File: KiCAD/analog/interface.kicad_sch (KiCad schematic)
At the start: 11 parts, among them J15 Conn_01x03_Pin, J4 8P8C_Shielded, U16 AM26LS32ACN

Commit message: schematic: revB encoder interrupt rerouted through CAT6 umbilical
- interface.kicad_sch: ENC_INT global label (input) replaces the old
  direct wire+GND stub; encoder interrupt now travels over the RJ45
  cable with the shield as signal return
- frontpanel.kicad_sch: 4-pin header J (Conn_01x04) added for up to
  3 encoder connections + one test-point pin; ENC_INT_IN label wired in
- arduino.kicad_sch: removed orphaned Conn_Coaxial symbol cache
- vfo.kicad_sch: minor layout/annotation updates

Co-Authored-By: Claude Sonnet 4.6 (1M context) <noreply@anthropic.com>
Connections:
- net GND: no longer J4.5
- new net ENC_INT: J4.5
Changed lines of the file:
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@@
 	(wire
 		(pts
-			(xy 64.77 91.44) (xy 64.77 95.25)
+			(xy 139.7 113.03) (xy 149.86 113.03)
 		)
 		(stroke
@@
 	(wire
 		(pts
-			(xy 139.7 113.03) (xy 149.86 113.03)
+			(xy 170.18 92.71) (xy 142.24 92.71)
 		)
 		(stroke
@@
 	(wire
 		(pts
-			(xy 170.18 92.71) (xy 142.24 92.71)
+			(xy 35.56 96.52) (xy 58.42 96.52)
 		)
 		(stroke
@@
 	(wire
 		(pts
-			(xy 35.56 96.52) (xy 58.42 96.52)
+			(xy 142.24 92.71) (xy 137.16 92.71)
 		)
 		(stroke
@@
 	(wire
 		(pts
-			(xy 142.24 92.71) (xy 137.16 92.71)
+			(xy 153.67 97.79) (xy 151.13 97.79)
 		)
 		(stroke
@@
 	(wire
 		(pts
-			(xy 153.67 97.79) (xy 151.13 97.79)
+			(xy 151.13 105.41) (xy 151.13 97.79)
 		)
 		(stroke
@@
 	(wire
 		(pts
-			(xy 151.13 105.41) (xy 151.13 97.79)
+			(xy 35.56 88.9) (xy 82.55 88.9)
 		)
 		(stroke
@@
 	(wire
 		(pts
-			(xy 35.56 88.9) (xy 82.55 88.9)
+			(xy 60.96 71.12) (xy 83.82 71.12)
 		)
 		(stroke
@@
 	(wire
 		(pts
-			(xy 60.96 71.12) (xy 83.82 71.12)
+			(xy 58.42 135.89) (xy 91.44 135.89)
 		)
 		(stroke
@@
 	(wire
 		(pts
-			(xy 58.42 135.89) (xy 91.44 135.89)
+			(xy 142.24 97.79) (xy 137.16 97.79)
 		)
 		(stroke
@@
 	(wire
 		(pts
-			(xy 142.24 97.79) (xy 137.16 97.79)
+			(xy 58.42 96.52) (xy 58.42 135.89)
 		)
 		(stroke
@@
 	(wire
 		(pts
-			(xy 58.42 96.52) (xy 58.42 135.89)
+			(xy 170.18 105.41) (xy 151.13 105.41)
 		)
 		(stroke
@@
 	(wire
 		(pts
-			(xy 170.18 105.41) (xy 151.13 105.41)
+			(xy 77.47 83.82) (xy 77.47 78.74)
 		)
 		(stroke
@@
 		)
 	)
-	(wire
-		(pts
-			(xy 35.56 91.44) (xy 64.77 91.44)
-		)
-		(stroke
-			(width 0)
-			(type default)
-		)
-	)
-	(wire
-		(pts
-			(xy 77.47 83.82) (xy 77.47 78.74)
-		)
-		(stroke
-			(width 0)
-			(type default)
-		)
-	)
 	(global_label "MBL_B_P"
 		(shape output)
@@
 					(size 1.27 1.27)
 				)
+			)
+		)
+	)
+	(global_label "ENC_INT"
+		(shape input)
+		(at 35.56 91.44 0)
+		(fields_autoplaced yes)
+		(effects
+			(font
+				(size 1.27 1.27)
+			)
+			(justify left)
+		)
+		(property "Intersheetrefs" "${INTERSHEET_REFS}"
+			(at 46.1652 91.44 0)
+			(hide yes)
+			(show_name no)
+			(do_not_autoplace no)
+			(effects
+				(font
+					(size 1.27 1.27)
+				)
+				(justify left)
 			)
 		)
@@
 					(unit 1)
 				)
-			)
-		)
-	)
-	(symbol
-		(lib_id "power:GND")
-		(at 64.77 95.25 0)
-		(unit 1)
-		(body_style 1)
-		(exclude_from_sim no)
-		(in_bom yes)
-		(on_board yes)
-		(in_pos_files yes)
-		(dnp no)
-		(fields_autoplaced yes)
-		(property "Reference" "#PWR090"
-			(at 64.77 101.6 0)
-			(hide yes)
-			(show_name no)
-			(do_not_autoplace no)
-			(effects
-				(font
-					(size 1.27 1.27)
-				)
-			)
-		)
-		(property "Value" "GND"
-			(at 64.77 100.33 0)
-			(show_name no)
-			(do_not_autoplace no)
-			(effects
-				(font
-					(size 1.27 1.27)
-				)
-			)
-		)
-		(property "Footprint" ""
-			(at 64.77 95.25 0)
-			(hide yes)
-			(show_name no)
-			(do_not_autoplace no)
-			(effects
-				(font
-					(size 1.27 1.27)
-				)
-			)
-		)
-		(property "Datasheet" ""
-			(at 64.77 95.25 0)
-			(hide yes)
-			(show_name no)
-			(do_not_autoplace no)
-			(effects
-				(font
-					(size 1.27 1.27)
-				)
-			)
-		)
-		(property "Description" "Power symbol creates a global label with name \"GND\" , ground"
-			(at 64.77 95.25 0)
-			(hide yes)
-			(show_name no)
-			(do_not_autoplace no)
-			(effects
-				(font
-					(size 1.27 1.27)
-				)
-			)
-		)
-		(pin "1"
-		)
-		(instances
-			(project "analog"
-				(path "/d3de40b8-856b-4fbd-829c-f45ffcd55742/5c3f4a2b-7d1e-4f8b-9c6d-0e8a1b2c3d4e"
-					(reference "#PWR090")
-					(unit 1)
-				)

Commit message: kicad: fix AM26LS32ACN (U16) symbol pin assignments
Correct four pin numbers that were wrong in both the library symbol
and the interface.kicad_sch embedded lib_symbols copy:

  1B: 3 -> 1   1Y: 1 -> 3
  4B: 13 -> 15  4Y: 15 -> 13

1A (pin 2), 4A (pin 14), and all other pins were correct.
RevB PCB layout will pick up the corrected netlist automatically.

Co-Authored-By: Claude Sonnet 4.6 <noreply@anthropic.com>
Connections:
- net MBL_A_N: now also U16.1 (1B); no longer U16.3 (1B)
- net at R26.1: now also U16.3 (1Y); no longer U16.1 (1Y)

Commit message: KiCad revB: protoshield schematic complete + 1N4728A symbol + misc board edits
Protoshield (Metro ESP32-S3 GPIO signal conditioning):
- Full schematic drawn: series R + bypass C + Zener clamp for I_CATHODE_A/B
  (1k+100nF+1N4728A), MBL600_A/B (10k/20k divider + 22pF), GRID_BLOCK_CRASH
  (1k+100nF), ENC_INT (330R+10k pull-up), PADDLE_A/B (10k pull-ups), RESET_N
  (100nF), TR_SENSE (10k pull-up), passthrough nodes for SPI and LDAC_4728
- All THT footprints assigned (ceramic disc caps, DIN0207 resistors, Phoenix
  MKDS-1.5 2-pin/3-pin terminal blocks)
- ENC_INT wiring gap fixed (R7 re-placed to connect J4 pin 2 to ENC_INT net)
- sym-lib-table added (points to shared xmitter.kicad_sym)
- protoshield.net generated netlist added for reference

Symbol library (xmitter.kicad_sym):
- Added 1N4728A (3.3V 1W Zener, DO-41) with correct KiCad 9.0 inline pts format

Other boards:
- analog/arduino.kicad_sch: minor junction/reference adjustments after Metro
  symbol was removed to protoshield in prior session
- bias: kicad_pro and kicad_sch updated (ongoing schematic work)
- power/sym-lib-table added for new stub project

Added: Purchase Orders (JLCPCB + Digi-Key invoices), tools/_scan_symbols.py

Co-Authored-By: Claude Sonnet 4.6 <noreply@anthropic.com>
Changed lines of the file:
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@@
 		(in_pos_files yes)
 		(dnp no)
-		(fields_autoplaced yes)
 		(property "Reference" "#PWR099"
 			(at 142.24 111.76 0)
@@
 		)
 		(property "Value" "GND"
-			(at 142.24 110.49 0)
+			(at 145.796 108.204 0)
 			(show_name no)
 			(do_not_autoplace no)

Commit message: KiCad revB: schematic review pass — I2C, ENC_INT, GND returns, GRID_BLOCK_CRASH clamp
Result of extended review pass against fresh netlists across all four
boards. All connectivity blockers resolved.

- Si5351 SDA/SCL wired via 0R jumpers (R8/R9) puts I2C on PCB traces
  for PCF8575 U17 and the RJ45 to the front panel. MCP4728 side has
  parallel 0R jumpers (R3/R4/R5) left DNP by default — STEMMA-QT is
  the intended path.
- ENC_INT chain unified end-to-end with staged names:
  ENC_INT_RAW (frontpanel encoder wire-OR) → ENC_INT_CLEAN (across
  CAT + analog pass-through) → ENC_INT_FINAL (post-protoshield
  conditioning). Frontpanel U4 (MCP1700-3.3 LDO) sources the +3.3V
  the pull-up R4 needs; pull-up moved to encoder side for sharper
  falling edges over the 2 m CAT run.
- Protoshield GRID_BLOCK_CRASH gets 1N4728A Zener clamp (D5),
  matching the I_CATHODE and MBL600 5V→3.3V clamp topology.
- Protoshield MBL600 conditioning rebuilt: 1K series + 100nF filter
  + 1N4728A clamp (was 10K/20K divider + 22pF that filtered nothing
  below RF).
- PADDLE_A/B and RESET_N removed from analog board — case-mounted
  switches wire directly to protoshield.
- Protoshield J1/J6 widened to 3-pin to include GND returns for the
  case-mounted paddle and reset switches.
- Bias board reference designators reorganized functionally
  (R_FA/R_FB feedback, R_GA/R_GB gain, R_PADA/R_PADB, R_GLA/R_GLB
  grid line, R_GATE, R_Z).
- New Documentation/control_board_functional_blocks.md captures
  KeyUp/Gate 2 keying, relay assignments (J6=T/R, J7=HV primary,
  J8=HV inrush), CD14538B heartbeat watchdog, TR_SENSE interlock,
  and J13 power-migration header.
- Fresh netlists exported for all four boards.

Co-Authored-By: Claude Opus 4.7 <noreply@anthropic.com>
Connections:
- net ENC_INT renamed ENC_INT_CLEAN
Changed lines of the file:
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@@
 		)
 	)
-	(global_label "ENC_INT"
-		(shape input)
+	(global_label "ENC_INT_CLEAN"
+		(shape output)
 		(at 35.56 91.44 0)
 		(fields_autoplaced yes)
@@
 		)
 		(property "Intersheetrefs" "${INTERSHEET_REFS}"
-			(at 46.1652 91.44 0)
+			(at 52.999 91.44 0)
 			(hide yes)
 			(show_name no)

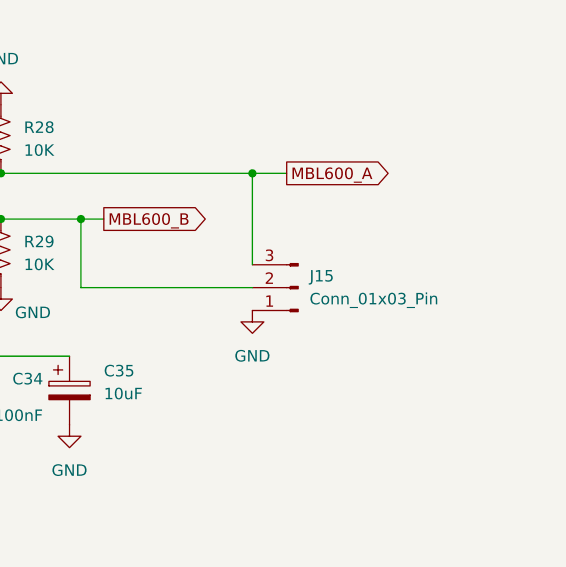
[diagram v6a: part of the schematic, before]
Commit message: revC: accumulated schematic/netlist updates + BOM tooling
- analog + ss_pa netlists regenerated to current schematic state
- interface/arduino/dac/power sheet updates on analog
- fault_shutdown and pa_stage edits on ss_pa (footprint assignments)
- assign_cap_footprints.py: additional VALUE_TO_FOOTPRINT entries
- gen_board_boms.py: per-board BOM generator (multi-sheet .xlsx by
  component category, first-match-wins bucketing, DNP exclusion)
- gen_total_bom.py: consolidated BOM across analog + frontpanel + ss_pa
  for a single Mouser order, board-prefixed references, mixed-footprint
  flagging per Value row

Co-Authored-By: Claude Opus 4.7 <noreply@anthropic.com>
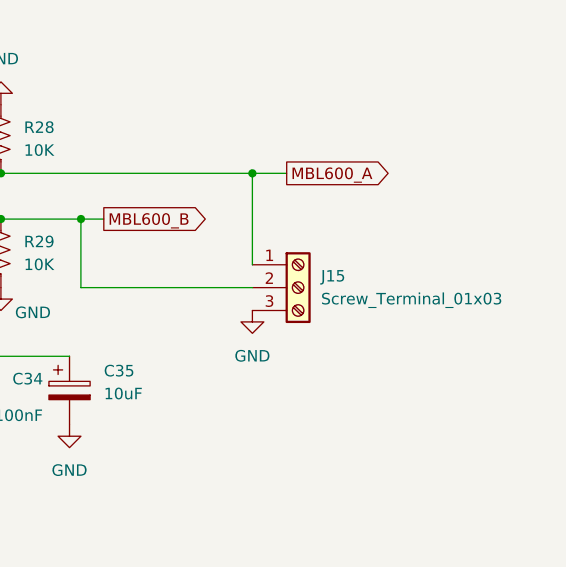
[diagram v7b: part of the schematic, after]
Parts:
- removed J15: Conn_01x03_Pin, Connector_PinHeader_2.54mm:PinHeader_1x03_P2.54mm_Vertical, symbol Connector:Conn_01x03_Pin
- added J15: Screw_Terminal_01x03, TerminalBlock_Phoenix:TerminalBlock_Phoenix_MKDS-1,5-3_1x03_P5.00mm_Horizontal, symbol Connector:Screw_Terminal_01x03
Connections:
- net GND: now also J15.3 (Pin_3)
- net MBL600_A: now also J15.1 (Pin_1)
- net MBL600_B: now also J15.2 (Pin_2)
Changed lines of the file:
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@@
+	)
+	(symbol
+		(lib_id "Connector:Screw_Terminal_01x03")
+		(at 175.26 105.41 0)
+		(unit 1)
+		(body_style 1)
+		(exclude_from_sim no)
+		(in_bom yes)
+		(on_board yes)
+		(in_pos_files yes)
+		(dnp no)
+		(fields_autoplaced yes)
+		(property "Reference" "J15"
+			(at 177.8 104.1399 0)
+			(show_name no)
+			(do_not_autoplace no)
+			(effects
+				(font
+					(size 1.27 1.27)
+				)
+				(justify left)
+			)
+		)
+		(property "Value" "Screw_Terminal_01x03"
+			(at 177.8 106.6799 0)
+			(show_name no)
+			(do_not_autoplace no)
+			(effects
+				(font
+					(size 1.27 1.27)
+				)
+				(justify left)
+			)
+		)
+		(property "Footprint" "TerminalBlock_Phoenix:TerminalBlock_Phoenix_MKDS-1,5-3_1x03_P5.00mm_Horizontal"
+			(at 175.26 105.41 0)
+			(hide yes)
+			(show_name no)
+			(do_not_autoplace no)
+			(effects
+				(font
+					(size 1.27 1.27)
+				)
+			)
+		)
+		(property "Datasheet" ""
+			(at 175.26 105.41 0)
+			(hide yes)
+			(show_name no)
+			(do_not_autoplace no)
+			(effects
+				(font
+					(size 1.27 1.27)
+				)
+			)
+		)
+		(property "Description" "Generic screw terminal, single row, 01x03, script generated (kicad-library-utils/schlib/autogen/connector/)"
+			(at 175.26 105.41 0)
+			(hide yes)
+			(show_name no)
+			(do_not_autoplace no)
+			(effects
+				(font
+					(size 1.27 1.27)
+				)
+			)
+		)
+		(pin "1"
+		)
+		(pin "2"
+		)
+		(pin "3"
+		)
+		(instances
+			(project "analog"
+				(path "/d3de40b8-856b-4fbd-829c-f45ffcd55742/5c3f4a2b-7d1e-4f8b-9c6d-0e8a1b2c3d4e"
+					(reference "J15")
+					(unit 1)
+				)
+			)
+		)
 	)
 	(symbol
@@
 					(unit 1)
 				)
-			)
-		)
-	)
-	(symbol
-		(lib_id "Connector:Conn_01x03_Pin")
-		(at 175.26 105.41 180)
-		(unit 1)
-		(body_style 1)
-		(exclude_from_sim no)
-		(in_bom yes)
-		(on_board yes)
-		(in_pos_files yes)
-		(dnp no)
-		(fields_autoplaced yes)
-		(property "Reference" "J15"
-			(at 176.53 104.1399 0)
-			(show_name no)
-			(do_not_autoplace no)
-			(effects
-				(font
-					(size 1.27 1.27)
-				)
-				(justify right)
-			)
-		)
-		(property "Value" "Conn_01x03_Pin"
-			(at 176.53 106.6799 0)
-			(show_name no)
-			(do_not_autoplace no)
-			(effects
-				(font
-					(size 1.27 1.27)
-				)
-				(justify right)
-			)
-		)
-		(property "Footprint" "Connector_PinHeader_2.54mm:PinHeader_1x03_P2.54mm_Vertical"
-			(at 175.26 105.41 0)
-			(hide yes)
-			(show_name no)
-			(do_not_autoplace no)
-			(effects
-				(font
-					(size 1.27 1.27)
-				)
-			)
-		)
-		(property "Datasheet" ""
-			(at 175.26 105.41 0)
-			(hide yes)
-			(show_name no)
-			(do_not_autoplace no)
-			(effects
-				(font
-					(size 1.27 1.27)
-				)
-			)
-		)
-		(property "Description" "Generic connector, single row, 01x03, script generated"
-			(at 175.26 105.41 0)
-			(hide yes)
-			(show_name no)
-			(do_not_autoplace no)
-			(effects
-				(font
-					(size 1.27 1.27)
-				)
-			)
-		)
-		(pin "2"
-		)
-		(pin "1"
-		)
-		(pin "3"
-		)
-		(instances
-			(project "analog"
-				(path "/d3de40b8-856b-4fbd-829c-f45ffcd55742/5c3f4a2b-7d1e-4f8b-9c6d-0e8a1b2c3d4e"
-					(reference "J15")
-					(unit 1)
-				)

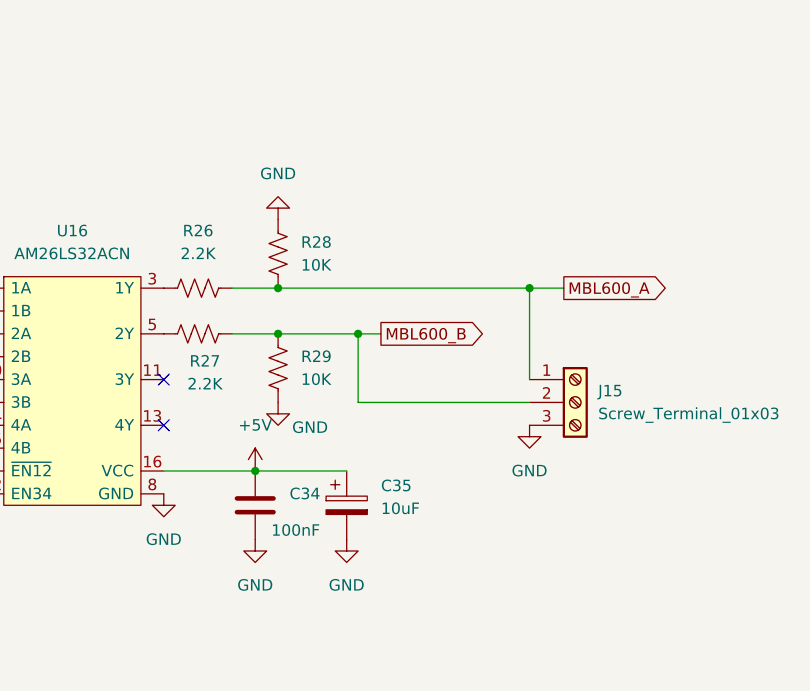
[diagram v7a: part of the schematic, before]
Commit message: revD analog: DGFET op-amp offset-mute topology + doc updates
Retire the Q11/Q12 PNP KeyUp mute path on the DGFET keyer G2 (sim showed
only ~2.6:1 on/off ratio with G1 biased above V_TO). Replace with an
LM7171 (U10) non-inverting op-amp wired as DC offset:
  V_G2 = V_DAC * (1 + R20/R23) - V_ref * (R20/R23)
with V_ref ~5.05V (1N4733A Zener D2, R24 1K bias, R25 1K / R32 100K
summing divider) and R20=6.2K / R23=10K (G=0.62). DAC=0 drives G2 to
-3.1V (fully cuts off the 40673, sim-verified 12pA leakage, ~10^9 on/off
ratio); DAC=5V drives G2 to +5V (matches prior keyed operating point).
KEY_UP net eliminated -- mute is intrinsic to the signal path, firmware
controls RF enable/disable solely via what it writes to the MCP4921
envelope channel.

Includes new test.kicad_sch sheet carrying the U10/R20-R32 subcircuit.

Doc updates: CLAUDE.md DGFET section rewritten; handoff doc gets a new
"DGFET keyer mute topology" section explaining retirement reason and
new transfer function; Master_Description Sec 2 and SPI-bus section
updated; revD_interconnect G2 amplitude-control block updated;
control_board_functional_blocks.md gets a prominent retirement banner
pointing at the current scheme.

Co-Authored-By: Claude Opus 4.7 <noreply@anthropic.com>
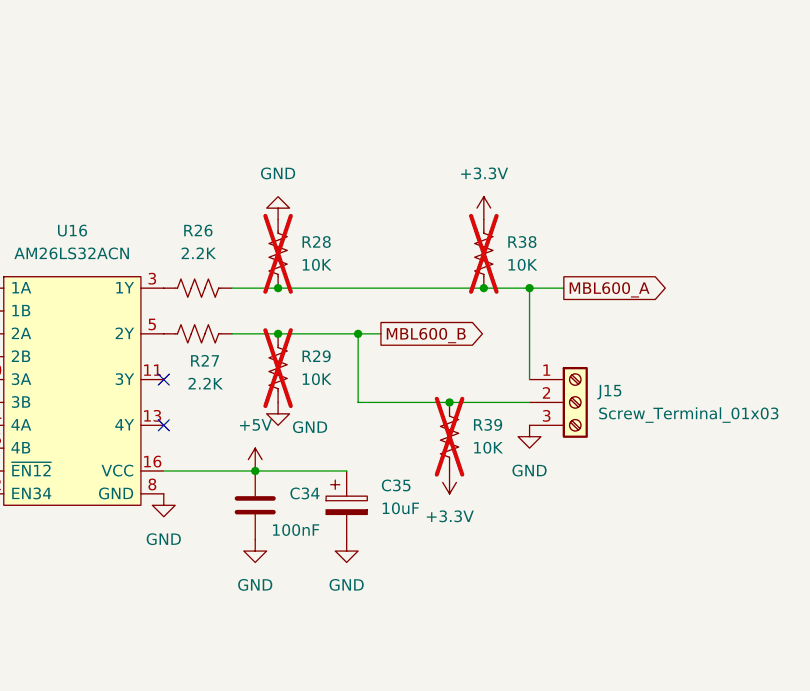
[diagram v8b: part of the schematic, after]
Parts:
- added R38, R39: 10K, symbol Device:R_US
- R28, R29: now not fitted
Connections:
- net MBL600_A: now also R38.2
- net MBL600_B: now also R39.1
- new net +3.3V: R38.1, R39.2
